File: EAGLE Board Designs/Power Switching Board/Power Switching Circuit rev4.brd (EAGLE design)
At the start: 160 x 100 mm, 64 parts, among them J1 CONNECTOR-4_SOURIAU_, J2 CONNECTOR-3_8STA20435PN, J3 CONNECTOR-4_SOURIAU_, K1 RELAY_SOLIDSTATE_NO_CMX60D20, Q1 TRANSISTOR_N_MOS_2-7K1S_TK100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, Q2 TRANSISTOR_N_MOS_2-7K1S_TK100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, Q3 TRANSISTOR_N_MOS_2-7K1S_TK100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, Q4 TRANSISTOR_N_MOS_2-7K1S_TK100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, U1 LTC4421

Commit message: Board design part 2
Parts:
- removed TP8: TEST_POINT, HyTechDevices:5015
- moved D6 93.7 mm to (26.7, 64.8), turned to 270 degrees
- moved TP9 88.0 mm to (38.1, 35.6)
- moved TP2 87.7 mm to (43.2, 43.2)
- moved TP3 82.3 mm to (33.0, 39.4)
- moved TP11 75.0 mm to (38.1, 43.2)
- moved TP1 74.8 mm to (43.2, 31.8)
- moved TP5 69.0 mm to (33.0, 43.2)
- moved TP12 68.7 mm to (33.0, 35.6)
- moved TP10 67.6 mm to (43.2, 35.6)
- moved TP7 65.6 mm to (38.1, 39.4)
- moved TP6 65.4 mm to (43.2, 39.4)
- moved D4 61.0 mm to (78.7, 41.9)
- moved D5 61.0 mm to (73.7, 41.9)
- moved TP4 57.8 mm to (38.1, 31.8)
- moved D3 48.9 mm to (78.7, 26.7), turned to 180 degrees
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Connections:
- removed net CONVOUT: TP8.1
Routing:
- net !SHDN: track 0.00 -> 109.7 mm, vias 0 -> 1
- net OUTPREFUSE: track 0.00 -> 89.4 mm
- net GND: track 0.00 -> 85.7 mm, vias 0 -> 10
- net DCDC_VICOR: track 0.00 -> 83.6 mm, vias 0 -> 1
- net GATE2: track 3.02 -> 81.4 mm, vias 0 -> 4
- net BATTERY: track 0.00 -> 73.3 mm, vias 0 -> 1
- net DCDC_VICORPREMOS: track 0.00 -> 66.4 mm, vias 0 -> 2
- net GATE1: track 0.00 -> 65.9 mm, vias 0 -> 4
- net BATTIN: track 12.1 -> 77.3 mm
- net SOURCE1: track 0.00 -> 64.5 mm, vias 0 -> 4
- net SOURCE2: track 3.28 -> 59.1 mm, vias 0 -> 2
- net N$20: track 0.00 -> 51.9 mm, vias 0 -> 2
- net N$18: track 0.00 -> 48.2 mm, vias 0 -> 2
- net OUT: track 0.00 -> 46.3 mm, vias 0 -> 3
- net N$31: track 0.00 -> 44.3 mm, vias 0 -> 2
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- added copper zone on layer 1, net BATTIN
- added copper zone on layer 1, net N$12
- added copper zone on layer 1, net SOURCE1

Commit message: Board design part 3
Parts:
- added U$1: (no value), HyTechManufacturing:LOGO_GT_LARGE
- added U$2: (no value), HyTechManufacturing:LOGO_HYTECH_MEDIUM
- added U$3, U$4, U$5, U$6: (no value), HyTechManufacturing:MOUNTING_M4
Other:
- board size 160 x 100 mm -> 100.3 x 100.1 mm
- board text added: "DO NOT INTALL XF2 UNLESS BYPASSING ENTIRE CIRCUIT!"
- board text added: "Power Switching Board rev4 Designed by Steven Elias"
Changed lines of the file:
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@@
 <board>
 <plain>
-<wire x1="0" y1="0" x2="160" y2="0" width="0" layer="20"/>
-<wire x1="160" y1="0" x2="160" y2="100" width="0" layer="20"/>
-<wire x1="160" y1="100" x2="0" y2="100" width="0" layer="20"/>
-<wire x1="0" y1="100" x2="0" y2="0" width="0" layer="20"/>
+<wire x1="0" y1="0" x2="100.31" y2="0" width="0" layer="20"/>
+<wire x1="100.31" y1="0" x2="100.31" y2="100" width="0" layer="20"/>
+<wire x1="100.31" y1="100" x2="0" y2="100.076" width="0" layer="20"/>
+<wire x1="0" y1="100.076" x2="0" y2="0" width="0" layer="20"/>
+<text x="52.07" y="6.35" size="1.778" layer="27" font="vector" align="bottom-center">Power Switching Board rev4
+Designed by
+Steven Elias</text>
+<text x="45.72" y="88.9" size="1.27" layer="27" font="vector" align="bottom-center">DO NOT INTALL XF2
+UNLESS BYPASSING
+ENTIRE CIRCUIT!</text>
 </plain>
 <attributes>
@@
 <attribute name="MOPN" value="534-3568" x="-11.43" y="22.86" size="1.778" layer="27" rot="R270" display="off"/>
 <attribute name="MPN" value="3568" x="-11.43" y="22.86" size="1.778" layer="27" rot="R270" display="off"/>
-<attribute name="NAME" x="59.69" y="78.74" size="0.8128" layer="25" font="vector" rot="R270" align="bottom-center"/>
+<attribute name="NAME" x="51.2064" y="78.6892" size="0.8128" layer="25" font="vector" rot="R270" align="bottom-center"/>
 </element>
 <element name="XF3" library="HyTechDevices" package="3568" value="FUSE_HOLDER_MINIBLADEPTH" x="71.12" y="67.31" smashed="yes">
@@
 <attribute name="MOPN" value="534-3568" x="-39.37" y="57.15" size="1.778" layer="27" rot="R270" display="off"/>
 <attribute name="MPN" value="3568" x="-39.37" y="57.15" size="1.778" layer="27" rot="R270" display="off"/>
-<attribute name="NAME" x="41.91" y="78.74" size="0.8128" layer="25" font="vector" rot="R270" align="bottom-center"/>
-</element>
+<attribute name="NAME" x="33.2232" y="78.74" size="0.8128" layer="25" font="vector" rot="R270" align="bottom-center"/>
+</element>
+<element name="U$1" library="HyTechManufacturing" package="LOGO_GT_LARGE" value="" x="21.59" y="11.43" smashed="yes"/>
+<element name="U$2" library="HyTechManufacturing" package="LOGO_HYTECH_MEDIUM" value="" x="27.94" y="19.05" smashed="yes"/>
+<element name="U$3" library="HyTechManufacturing" package="MOUNTING_M4" value="" x="7.62" y="68.58" smashed="yes"/>
+<element name="U$4" library="HyTechManufacturing" package="MOUNTING_M4" value="" x="6.35" y="6.35" smashed="yes"/>
+<element name="U$5" library="HyTechManufacturing" package="MOUNTING_M4" value="" x="92.71" y="93.98" smashed="yes"/>
+<element name="U$6" library="HyTechManufacturing" package="MOUNTING_M4" value="" x="92.71" y="6.35" smashed="yes"/>
 </elements>
 <signals>
@@
 <contactref element="TP6" pad="1"/>
 <polygon width="0.1524" layer="16" thermals="no">
-<vertex x="0" y="100.33"/>
+<vertex x="0" y="100.076"/>
 <vertex x="0" y="0"/>
-<vertex x="160.02" y="0"/>
-<vertex x="160.02" y="100.33"/>
+<vertex x="100.33" y="0"/>
+<vertex x="100.33" y="100.076"/>
 </polygon>
 <wire x1="21.59" y1="29.73" x2="21.578" y2="29.718" width="0.254" layer="1"/>
@@
 </board>
 </drawing>
+<compatibility>
+<note version="6.3" minversion="6.2.2" severity="warning">
+Since Version 6.2.2 text objects can contain more than one line,
+which will not be processed correctly with this version.
+</note>
+</compatibility>
 </eagle>

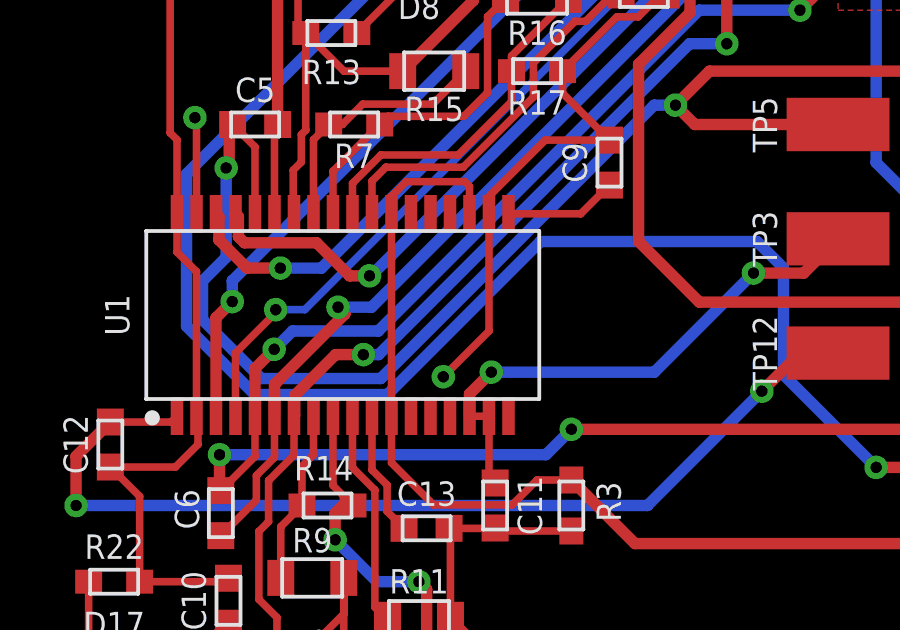
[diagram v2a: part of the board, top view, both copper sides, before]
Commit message: Connected Data Out pins to GND
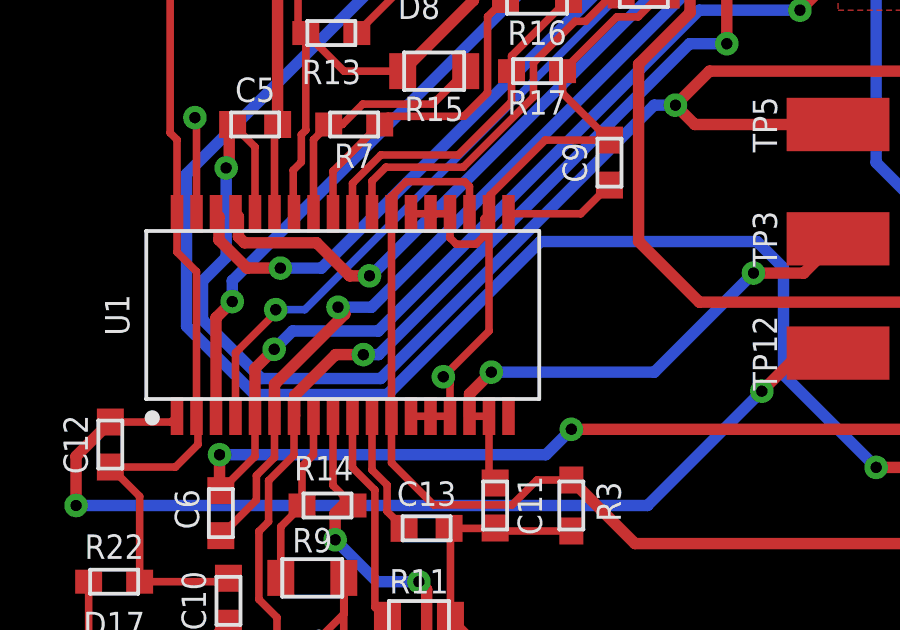
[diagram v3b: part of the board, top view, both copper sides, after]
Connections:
- net GND: now also U1.13, U1.14, U1.15, U1.22, U1.23, U1.24
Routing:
- net GND: track 85.7 -> 92.7 mm
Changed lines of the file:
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@@
 <wire x1="27.08813125" y1="47.498" x2="27.293" y2="47.498" width="0.254" layer="1"/>
 <wire x1="26.35873125" y1="46.7686" x2="27.08813125" y2="47.498" width="0.254" layer="1"/>
+<contactref element="U1" pad="14"/>
+<contactref element="U1" pad="23"/>
+<contactref element="U1" pad="13"/>
+<contactref element="U1" pad="24"/>
+<contactref element="U1" pad="15"/>
+<contactref element="U1" pad="22"/>
+<wire x1="21.385" y1="40.205" x2="21.2244" y2="40.0444" width="0.254" layer="1"/>
+<wire x1="21.2244" y1="40.0444" x2="21.2244" y2="39.46426875" width="0.254" layer="1"/>
+<wire x1="21.2244" y1="39.46426875" x2="20.95233125" y2="39.1922" width="0.254" layer="1"/>
+<wire x1="20.95233125" y1="39.1922" x2="20.2946" y2="39.1922" width="0.254" layer="1"/>
+<wire x1="20.2946" y1="39.1922" x2="20.085" y2="39.4018" width="0.254" layer="1"/>
+<wire x1="20.085" y1="39.4018" x2="20.085" y2="40.205" width="0.254" layer="1"/>
+<wire x1="20.085" y1="40.205" x2="19.435" y2="40.205" width="0.254" layer="1"/>
+<wire x1="19.435" y1="40.205" x2="18.785" y2="40.205" width="0.254" layer="1"/>
+<wire x1="18.785" y1="33.455" x2="19.435" y2="33.455" width="0.254" layer="1"/>
+<wire x1="19.435" y1="33.455" x2="20.085" y2="33.455" width="0.254" layer="1"/>
+<wire x1="20.085" y1="33.455" x2="20.085" y2="34.5504" width="0.254" layer="1"/>
+<wire x1="20.085" y1="34.5504" x2="19.8628" y2="34.7726" width="0.254" layer="1"/>
 </signal>
 <signal name="DCDC_VICORPREMOS">

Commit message: Final fixes of board
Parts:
- TP3: value TEST_POINT -> INTVDD
- U$1: device HyTechManufacturing:LOGO_GT_LARGE -> HyTechManufacturing:LOGO_GT_MEDIUM
- moved U$1 76.3 mm to (94.0, 35.6), turned to 90 degrees
- moved U$2 72.7 mm to (96.5, 43.2), turned to 90 degrees
- moved D8 38.6 mm to (30.5, 11.4), turned to 90 degrees
- moved D17 21.4 mm to (25.3, 11.4), turned to 90 degrees
- moved C1 14.0 mm to (77.5, 41.9)
- moved R11 14.0 mm to (19.1, 12.7)
- moved R8 14.0 mm to (15.4, 10.7)
- moved TP10 14.0 mm to (43.2, 21.6)
- moved TP12 14.0 mm to (33.0, 21.6)
- moved TP9 14.0 mm to (38.1, 21.6)
- moved C13 14.0 mm to (19.3, 15.7)
- moved R10 14.0 mm to (19.1, 9.91)
- moved R22 14.0 mm to (8.89, 14.0)
- moved R9 14.0 mm to (15.5, 14.1)
- moved C10 14.0 mm to (12.7, 13.3)
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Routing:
- net N$6: track 2.55 -> 41.2 mm, vias 0 -> 4
- net N$5: track 2.68 -> 29.0 mm
- net N$7: track 2.14 -> 15.7 mm
- net GATE1: track 65.9 -> 73.7 mm, vias 4 -> 3
- net GLVMS: track 18.6 -> 13.1 mm
- net N$22: track 9.62 -> 4.24 mm
- net !SHDN: track 109.7 -> 112.0 mm
- net SOURCE2: track 59.1 -> 57.9 mm
- net GATE2: track 81.4 -> 82.5 mm
- net START: track 14.2 -> 13.3 mm
- net DCDC_VICORPREMOS: track 66.4 -> 67.1 mm
- net GND: track 92.7 -> 92.0 mm
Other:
- board size 100.3 x 100.1 mm -> 100.3 x 86.1 mm
- board text added: "BAT"
- board text added: "CPO"
- board text added: "DCDC"
- board text added: "G1"
- board text added: "G2"
- board text added: "GND"
- board text added: "HyTech Racing Power Switching Board rev4 Designed by Steven Elias"
- board text added: "INTVDD"
- board text added: "OUT"
- board text added: "S1"
- board text added: "S2"
- board text added: "SHDN!"
